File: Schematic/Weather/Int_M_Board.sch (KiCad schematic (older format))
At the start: 9 parts, among them J15 Conn_02x04_Odd_Even, U1 AMS1117

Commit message: more changes
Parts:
- added J24: Conn_01x05_Female, Connector_PinHeader_2.54mm:PinHeader_1x05_P2.54mm_Vertical, symbol Connector:Conn_01x05_Female
- added J25: Conn_01x04_Female, Connector_PinHeader_2.54mm:PinHeader_1x05_P2.54mm_Vertical, symbol Connector:Conn_01x04_Female
- renumbered C1 to C5, C2 to C6, C3 to C7, H17 to H19, H18 to H20, J15 to J23, R1 to R57, R2 to R58, U1 to U8
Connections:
- net J3_P5: now also J25.4 (Pin_4)
- net J2_P1 renamed J17_P2
- net J17_P2: now also J25.2 (Pin_2)
- net J2_P2 renamed J17_P1
- net J17_P1: now also J25.1 (Pin_1)
- net J3_P3 renamed J17_P3
- net J17_P3: now also J25.3 (Pin_3)
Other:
- moved on the sheet: C5, C6, C7, H19, H20, J23, R57, R58, U8

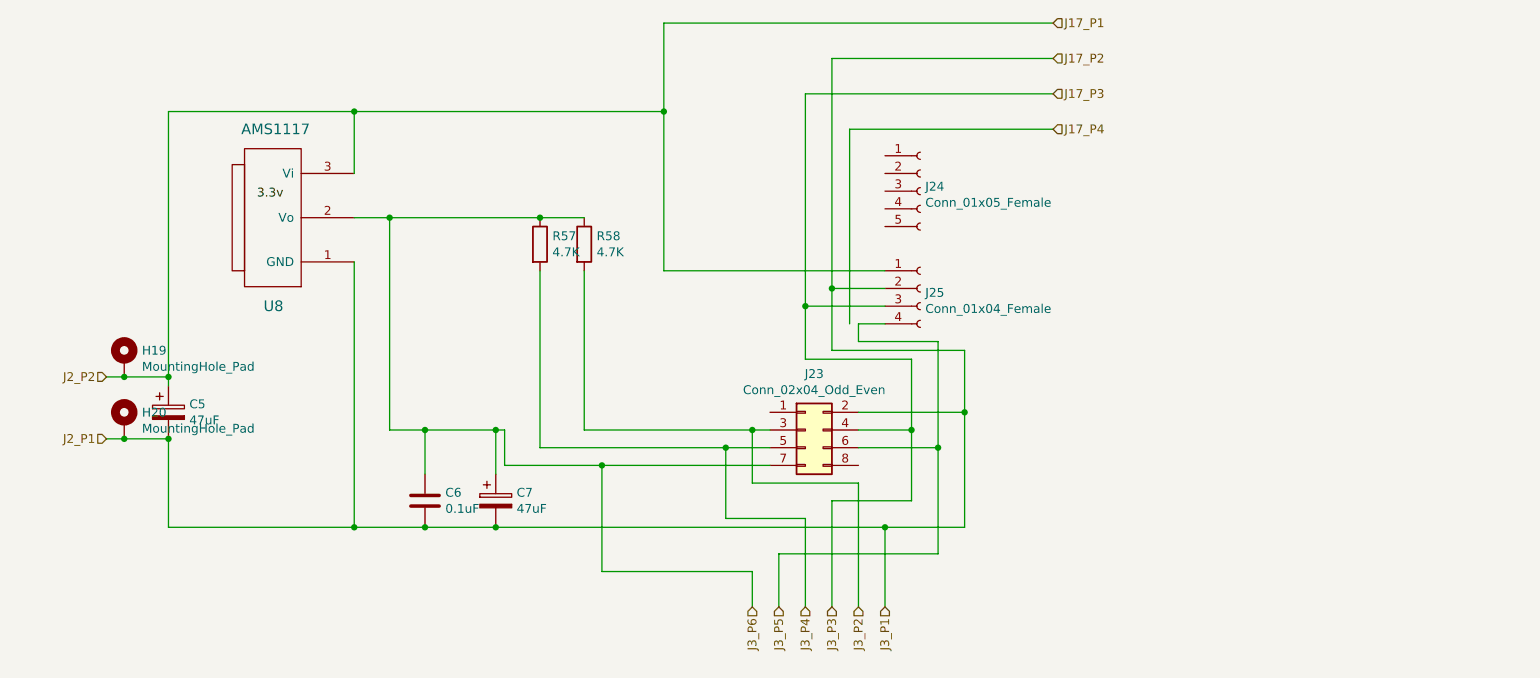
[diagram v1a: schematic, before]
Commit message: Connector relable start
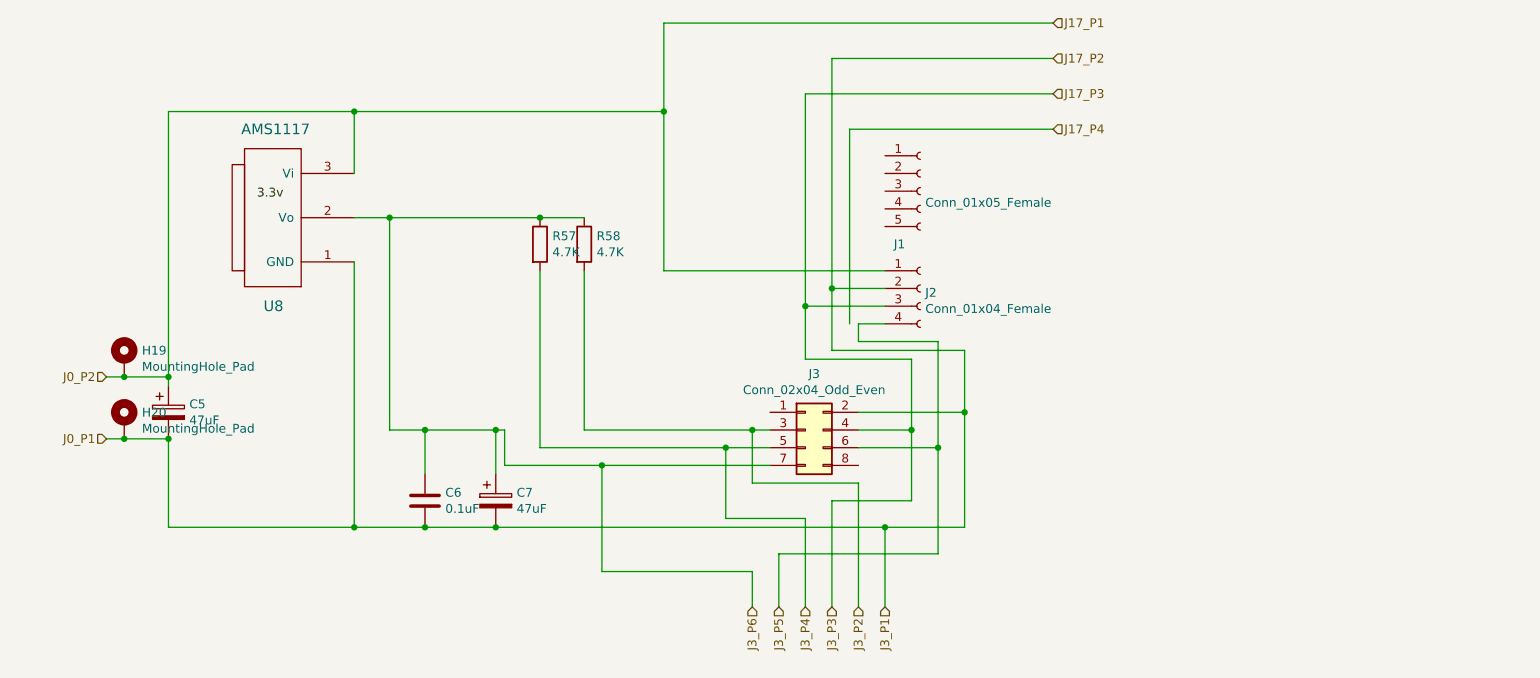
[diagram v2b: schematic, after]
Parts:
- renumbered J24 to J1, J25 to J2, J23 to J3
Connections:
- net J17_P1 renamed J0_P2
- net J17_P2 renamed J0_P1
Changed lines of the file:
@@
 $Descr A4 11693 8268
 encoding utf-8
-Sheet 14 15
+Sheet 13 15
 Title ""
 Date ""
@@
 $EndDescr
 Text HLabel 2600 3750 0    50   Input ~ 0
-J2_P1
+J0_P1
 Text HLabel 2600 3400 0    50   Input ~ 0
-J2_P2
+J0_P2
 Text HLabel 7000 4700 3    50   Input ~ 0
 J3_P1
@@
 	7450 3600 7450 4250
 $Comp
-L Connector_Generic:Conn_02x04_Odd_Even J23
+L Connector_Generic:Conn_02x04_Odd_Even J3
 U 1 1 5CB2F470
 P 6550 3700
-F 0 "J23" H 6600 4017 50  0000 C CNN
+F 0 "J3" H 6600 4017 50  0000 C CNN
 F 1 "Conn_02x04_Odd_Even" H 6600 3926 50  0000 C CNN
 F 2 "Connector_PinHeader_2.54mm:PinHeader_2x04_P2.54mm_Vertical" H 6550 3700 50  0001 C CNN
@@
 	6250 3700 5300 3700
 $Comp
-L Connector:Conn_01x04_Female J25
+L Connector:Conn_01x04_Female J2
 U 1 1 5CAF2DD7
 P 7200 2900
-F 0 "J25" H 7228 2876 50  0000 L CNN
+F 0 "J2" H 7228 2876 50  0000 L CNN
 F 1 "Conn_01x04_Female" H 7228 2785 50  0000 L CNN
 F 2 "Connector_PinHeader_2.54mm:PinHeader_1x05_P2.54mm_Vertical" H 7200 2900 50  0001 C CNN
@@
 Connection ~ 6550 3000
 $Comp
-L Connector:Conn_01x05_Female J24
+L Connector:Conn_01x05_Female J1
 U 1 1 5CB40D1B
 P 7200 2350
-F 0 "J24" H 7228 2376 50  0000 L CNN
+F 0 "J1" H 7050 2050 50  0000 L CNN
 F 1 "Conn_01x05_Female" H 7228 2285 50  0000 L CNN
 F 2 "Connector_PinHeader_2.54mm:PinHeader_1x05_P2.54mm_Vertical" H 7200 2350 50  0001 C CNN

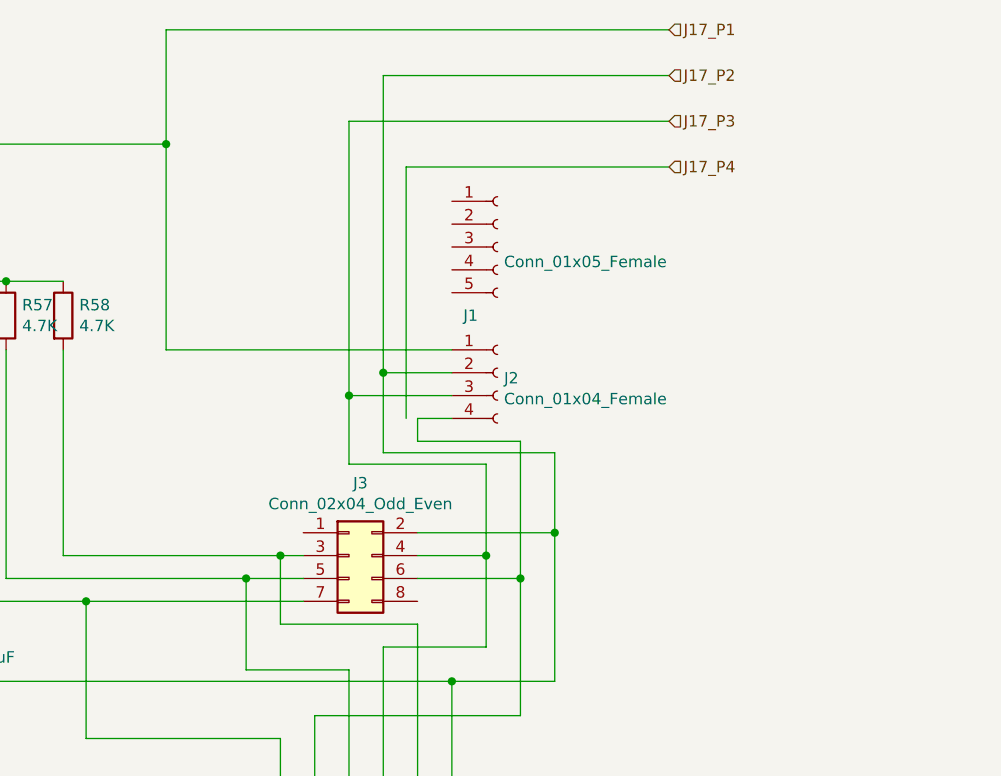
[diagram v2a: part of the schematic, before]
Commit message: Connector changes
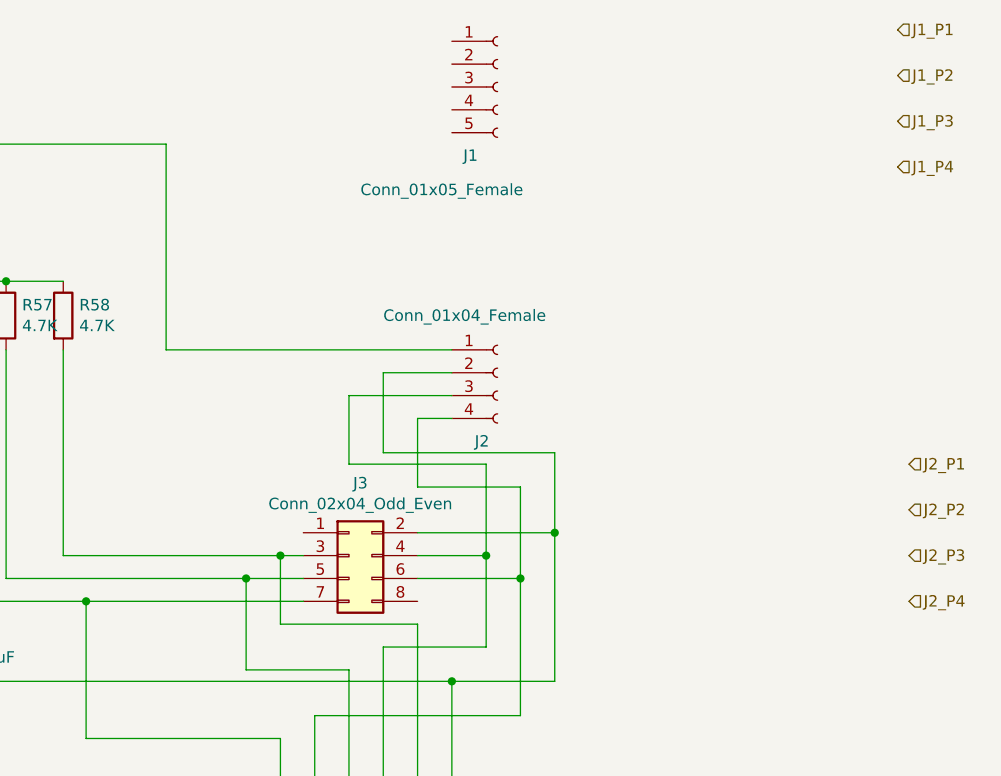
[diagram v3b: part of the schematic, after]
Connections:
- net J17_P3 renamed J3_P3
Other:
- moved on the sheet: J1
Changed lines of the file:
@@
 $Descr A4 11693 8268
 encoding utf-8
-Sheet 13 15
+Sheet 11 15
 Title ""
 Date ""
@@
 U 1 1 5CAF2DD7
 P 7200 2900
-F 0 "J2" H 7228 2876 50  0000 L CNN
-F 1 "Conn_01x04_Female" H 7228 2785 50  0000 L CNN
+F 0 "J2" H 7100 2600 50  0000 L CNN
+F 1 "Conn_01x04_Female" H 6700 3150 50  0000 L CNN
 F 2 "Connector_PinHeader_2.54mm:PinHeader_1x05_P2.54mm_Vertical" H 7200 2900 50  0001 C CNN
 F 3 "~" H 7200 2900 50  0001 C CNN
@@
 Connection ~ 7450 3600
 Wire Wire Line
-	7300 3800 7300 3200
-Wire Wire Line
-	7300 3200 6850 3200
-Wire Wire Line
-	6850 3200 6850 3100
-Wire Wire Line
 	6850 3100 7000 3100
-Connection ~ 7300 3800
 Wire Wire Line
 	7150 3700 7150 3300
@@
 Wire Wire Line
 	4800 4250 7000 4250
-Text HLabel 7950 1400 2    50   Input ~ 0
-J17_P1
-Text HLabel 7950 1600 2    50   Input ~ 0
-J17_P2
-Text HLabel 7950 1800 2    50   Input ~ 0
-J17_P3
-Text HLabel 7950 2000 2    50   Input ~ 0
-J17_P4
-Wire Wire Line
-	5750 1900 5750 1400
-Wire Wire Line
-	5750 1400 7950 1400
-Connection ~ 5750 1900
-Wire Wire Line
-	6700 2900 6700 1600
-Wire Wire Line
-	6700 1600 7950 1600
-Connection ~ 6700 2900
-Wire Wire Line
-	6800 3100 6800 2000
-Wire Wire Line
-	6800 2000 7950 2000
-Wire Wire Line
-	6550 3000 6550 1800
-Wire Wire Line
-	6550 1800 7950 1800
-Connection ~ 6550 3000
+Text HLabel 8950 1400 2    50   Input ~ 0
+J1_P1
+Text HLabel 8950 1600 2    50   Input ~ 0
+J1_P2
+Text HLabel 8950 1800 2    50   Input ~ 0
+J1_P3
+Text HLabel 8950 2000 2    50   Input ~ 0
+J1_P4
 $Comp
 L Connector:Conn_01x05_Female J1
 U 1 1 5CB40D1B
-P 7200 2350
-F 0 "J1" H 7050 2050 50  0000 L CNN
-F 1 "Conn_01x05_Female" H 7228 2285 50  0000 L CNN
-F 2 "Connector_PinHeader_2.54mm:PinHeader_1x05_P2.54mm_Vertical" H 7200 2350 50  0001 C CNN
-F 3 "~" H 7200 2350 50  0001 C CNN
-	1    7200 2350
-	1    0    0    -1
-$EndComp
+P 7200 1650
+F 0 "J1" H 7050 1350 50  0000 L CNN
+F 1 "Conn_01x05_Female" H 6600 1200 50  0000 L CNN
+F 2 "Connector_PinHeader_2.54mm:PinHeader_1x05_P2.54mm_Vertical" H 7200 1650 50  0001 C CNN
+F 3 "~" H 7200 1650 50  0001 C CNN
+	1    7200 1650
+	1    0    0    -1
+$EndComp
+Text HLabel 9000 3300 2    50   Input ~ 0
+J2_P1
+Text HLabel 9000 3500 2    50   Input ~ 0
+J2_P2
+Text HLabel 9000 3700 2    50   Input ~ 0
+J2_P3
+Text HLabel 9000 3900 2    50   Input ~ 0
+J2_P4
+Connection ~ 7300 3800
+Wire Wire Line
+	7300 3800 7300 3400
+Wire Wire Line
+	6850 3400 7300 3400
+Wire Wire Line
+	6850 3100 6850 3400
 $EndSCHEMATC

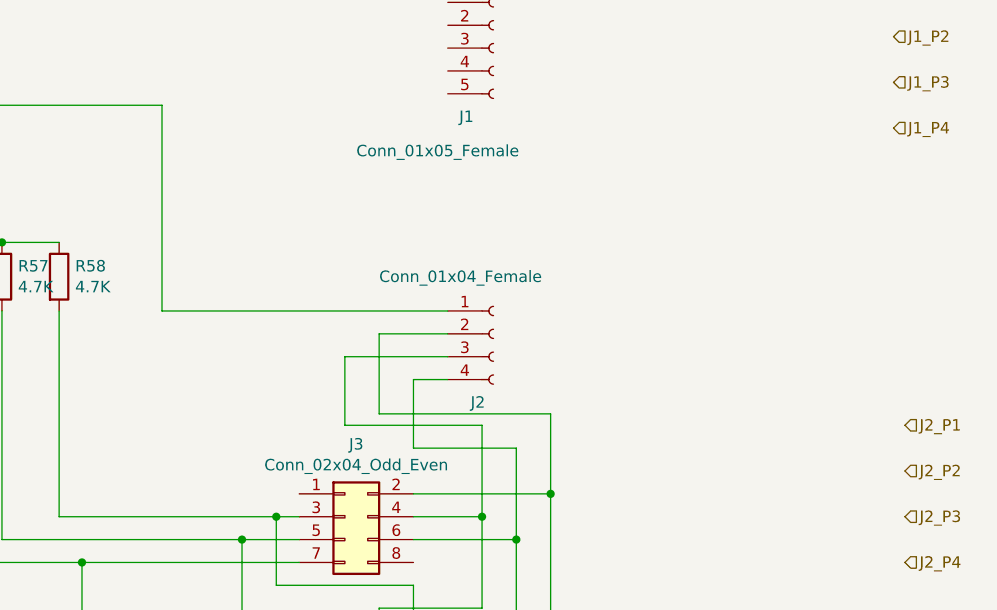
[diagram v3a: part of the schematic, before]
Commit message: config connectors sda scl
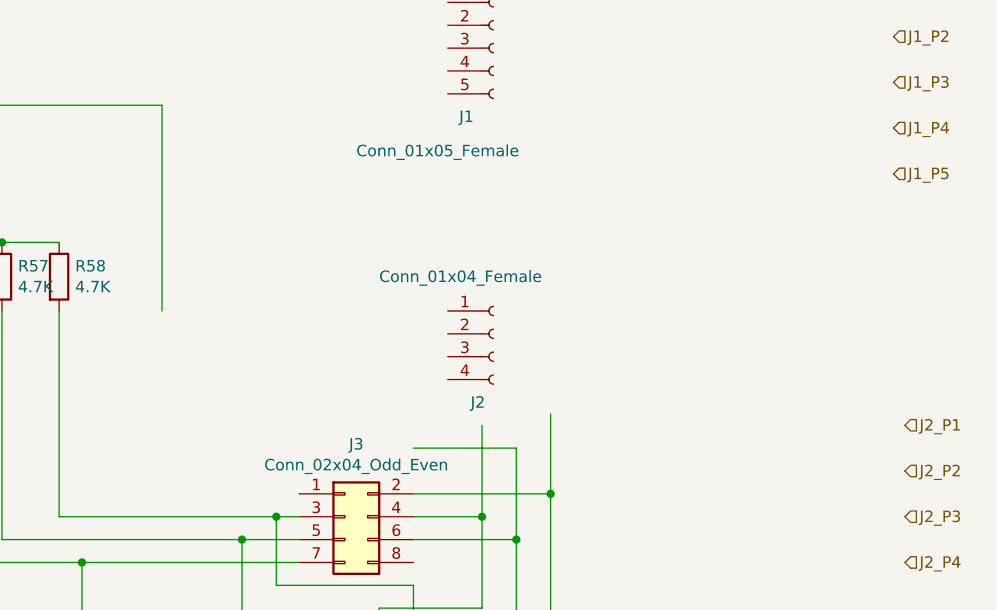
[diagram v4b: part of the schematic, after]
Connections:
- net labels added: J1_P5
- wire segments 68 -> 59
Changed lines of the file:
@@
 $EndComp
-Wire Wire Line
-	7000 2800 5750 2800
 Wire Wire Line
 	5750 1900 4000 1900
 Connection ~ 4000 1900
 Wire Wire Line
-	7000 2900 6700 2900
-Wire Wire Line
-	6700 2900 6700 3250
-Wire Wire Line
-	6700 3250 7450 3250
-Wire Wire Line
 	7450 3250 7450 3600
 Connection ~ 7450 3600
 Wire Wire Line
-	6850 3100 7000 3100
-Wire Wire Line
 	7150 3700 7150 3300
-Wire Wire Line
-	7150 3300 6550 3300
-Wire Wire Line
-	6550 3300 6550 3000
-Wire Wire Line
-	6550 3000 7000 3000
 Connection ~ 7150 3700
 Wire Wire Line
@@
 Wire Wire Line
 	6850 3400 7300 3400
-Wire Wire Line
-	6850 3100 6850 3400
+Text HLabel 8950 2200 2    50   Input ~ 0
+J1_P5
 $EndSCHEMATC
